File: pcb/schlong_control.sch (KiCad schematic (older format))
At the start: 38 parts, among them P1 Power Connector (120V AC), P2 Input, P3 Output, U1 74HC595, U2 MOC3063M, U3 MOC3063M, U4 MOC3063M, U5 MOC3063M, U6 MOC3063M, U7 LM7805

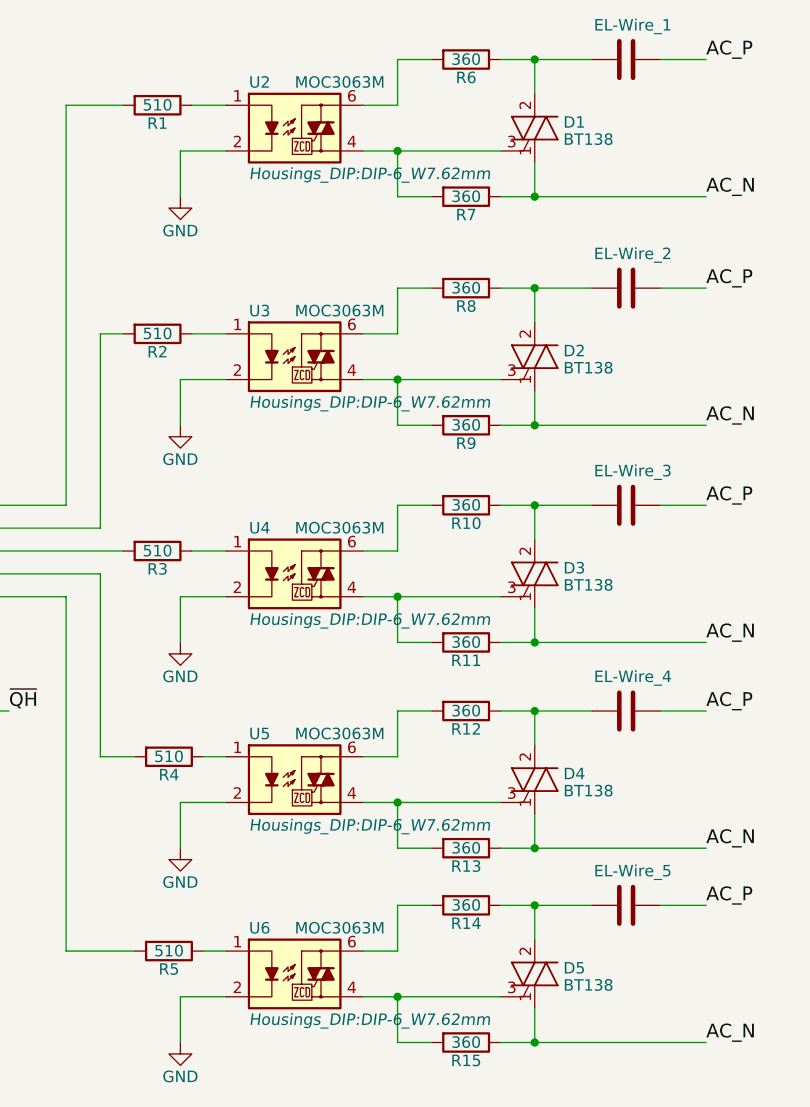
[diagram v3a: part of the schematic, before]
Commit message: shinkify pcb even more + little fixes
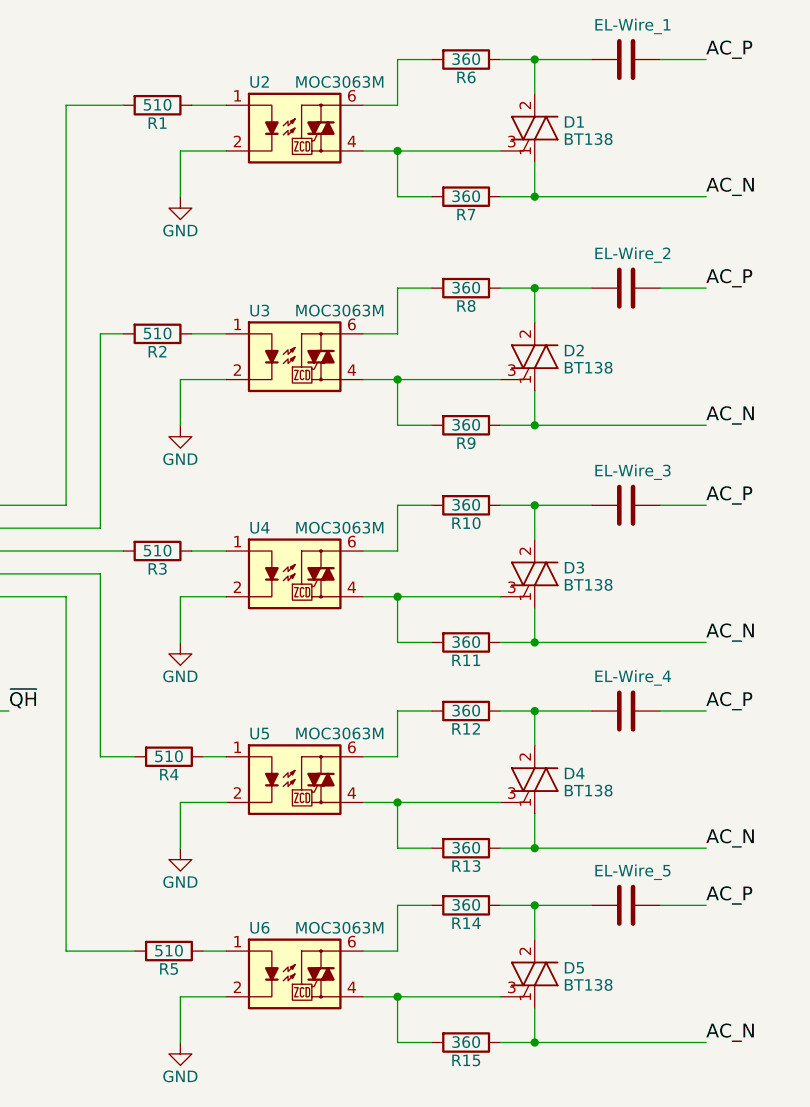
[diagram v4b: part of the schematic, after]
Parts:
- EL-Wire_1, EL-Wire_2, EL-Wire_3, EL-Wire_4, EL-Wire_5: footprint Connectors_Terminal_Blocks:TerminalBlock_Pheonix_MKDS1.5-2pol -> Connectors:PINHEAD1-2
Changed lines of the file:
@@
 EESchema Schematic File Version 2
-LIBS:schlong_control-rescue
 LIBS:power
 LIBS:device
@@
 LIBS:contrib
 LIBS:valves
+LIBS:bt138
+LIBS:7805_(enumerated_pins)
 LIBS:schlong_control-cache
 EELAYER 25 0
@@
 Sheet 1 1
 Title "Schlong Module Circuit"
-Date "2017-09-01"
-Rev "4"
+Date "2017-09-02"
+Rev "5"
 Comp "coon@c-base.org"
 Comment1 ""
@@
 F 0 "EL-Wire_1" V 6950 750 50  0000 L CNN
 F 1 "C" V 6850 800 50  0001 L CNN
-F 2 "Connectors_Terminal_Blocks:TerminalBlock_Pheonix_MKDS1.5-2pol" H 6838 800 50  0001 C CNN
+F 2 "Connectors:PINHEAD1-2" H 6838 800 50  0001 C CNN
 F 3 "" H 6800 950 50  0000 C CNN
 	1    6800 950
@@
 F 0 "EL-Wire_2" V 6950 1750 50  0000 L CNN
 F 1 "C" V 6850 1800 50  0001 L CNN
-F 2 "Connectors_Terminal_Blocks:TerminalBlock_Pheonix_MKDS1.5-2pol" H 6838 1800 50  0001 C CNN
+F 2 "Connectors:PINHEAD1-2" H 6838 1800 50  0001 C CNN
 F 3 "" H 6800 1950 50  0000 C CNN
 	1    6800 1950
@@
 F 0 "EL-Wire_3" V 6950 2700 50  0000 L CNN
 F 1 "C" V 6850 2750 50  0001 L CNN
-F 2 "Connectors_Terminal_Blocks:TerminalBlock_Pheonix_MKDS1.5-2pol" H 6838 2750 50  0001 C CNN
+F 2 "Connectors:PINHEAD1-2" H 6838 2750 50  0001 C CNN
 F 3 "" H 6800 2900 50  0000 C CNN
 	1    6800 2900
@@
 F 0 "EL-Wire_4" V 6950 3600 50  0000 L CNN
 F 1 "C" V 6850 3650 50  0001 L CNN
-F 2 "Connectors_Terminal_Blocks:TerminalBlock_Pheonix_MKDS1.5-2pol" H 6838 3650 50  0001 C CNN
+F 2 "Connectors:PINHEAD1-2" H 6838 3650 50  0001 C CNN
 F 3 "" H 6800 3800 50  0000 C CNN
 	1    6800 3800
@@
 F 0 "EL-Wire_5" V 6950 4450 50  0000 L CNN
 F 1 "C" V 6850 4500 50  0001 L CNN
-F 2 "Connectors_Terminal_Blocks:TerminalBlock_Pheonix_MKDS1.5-2pol" H 6838 4500 50  0001 C CNN
+F 2 "Connectors:PINHEAD1-2" H 6838 4500 50  0001 C CNN
 F 3 "" H 6800 4650 50  0000 C CNN
 	1    6800 4650
@@
 F 0 "U2" H 5150 1450 50  0000 L CNN
 F 1 "MOC3063M" H 5350 1450 50  0000 L CNN
-F 2 "Housings_DIP:DIP-6_W7.62mm" H 5150 1050 50  0000 L CIN
+F 2 "Housings_DIP:DIP-6_W7.62mm" H 5150 1050 50  0001 L CIN
 F 3 "" H 5340 1250 50  0000 L CNN
 	1    5350 1250
@@
 F 0 "U3" H 5150 2450 50  0000 L CNN
 F 1 "MOC3063M" H 5350 2450 50  0000 L CNN
-F 2 "Housings_DIP:DIP-6_W7.62mm" H 5150 2050 50  0000 L CIN
+F 2 "Housings_DIP:DIP-6_W7.62mm" H 5150 2050 50  0001 L CIN
 F 3 "" H 5340 2250 50  0000 L CNN
 	1    5350 2250
@@
 F 0 "U4" H 5150 3400 50  0000 L CNN
 F 1 "MOC3063M" H 5350 3400 50  0000 L CNN
-F 2 "Housings_DIP:DIP-6_W7.62mm" H 5150 3000 50  0000 L CIN
+F 2 "Housings_DIP:DIP-6_W7.62mm" H 5150 3000 50  0001 L CIN
 F 3 "" H 5340 3200 50  0000 L CNN
 	1    5350 3200
@@
 F 0 "U5" H 5150 4300 50  0000 L CNN
 F 1 "MOC3063M" H 5350 4300 50  0000 L CNN
-F 2 "Housings_DIP:DIP-6_W7.62mm" H 5150 3900 50  0000 L CIN
+F 2 "Housings_DIP:DIP-6_W7.62mm" H 5150 3900 50  0001 L CIN
 F 3 "" H 5340 4100 50  0000 L CNN
 	1    5350 4100
@@
 F 0 "U6" H 5150 5150 50  0000 L CNN
 F 1 "MOC3063M" H 5350 5150 50  0000 L CNN
-F 2 "Housings_DIP:DIP-6_W7.62mm" H 5150 4750 50  0000 L CIN
+F 2 "Housings_DIP:DIP-6_W7.62mm" H 5150 4750 50  0001 L CIN
 F 3 "" H 5340 4950 50  0000 L CNN
 	1    5350 4950

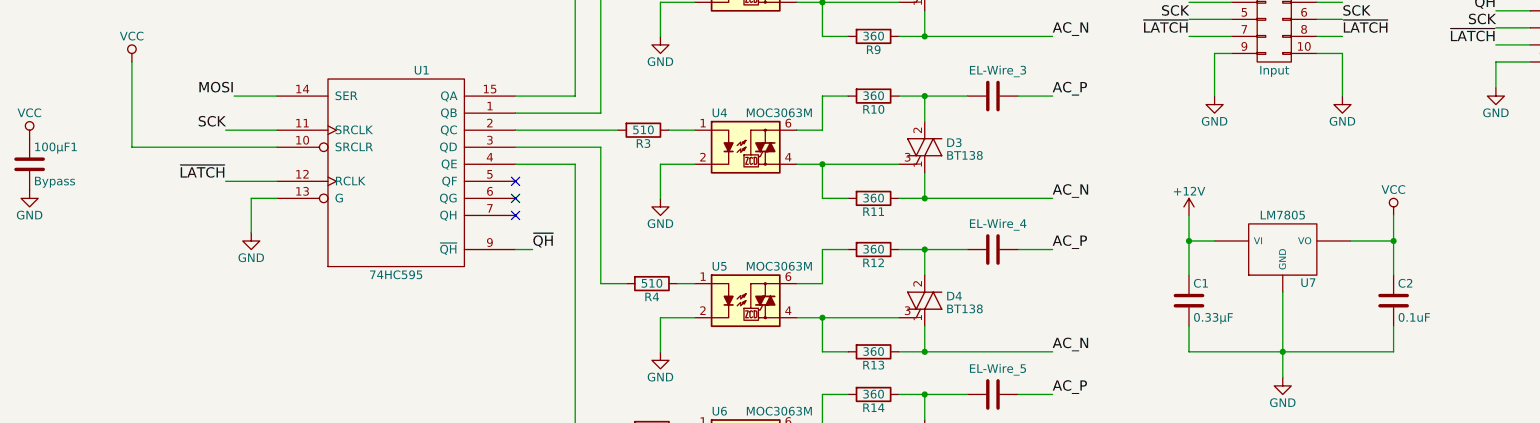
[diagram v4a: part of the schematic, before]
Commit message: redo routing (seperate logic voltage from AC voltage)
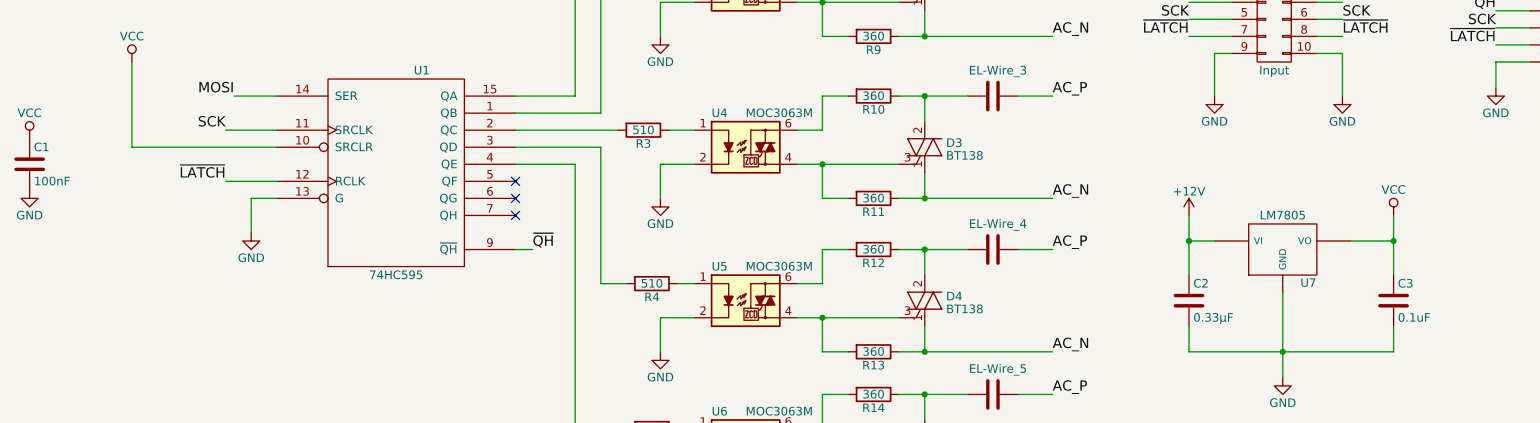
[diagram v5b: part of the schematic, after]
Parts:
- C1: renamed from 100µF1; value Bypass -> 100nF; footprint Capacitors_THT:C_Disc_D3.0mm_W1.6mm_P2.50mm -> Capacitors_ThroughHole:C_Disc_D3.0mm_W1.6mm_P2.50mm
- C2: renamed from C1; footprint Capacitors_THT:CP_Radial_D4.0mm_P1.50mm -> Capacitors_ThroughHole:CP_Radial_D4.0mm_P1.50mm
- C3: renamed from C2; footprint Capacitors_THT:CP_Radial_D4.0mm_P1.50mm -> Capacitors_ThroughHole:CP_Radial_D4.0mm_P1.50mm
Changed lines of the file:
@@
 AC_P
 $Comp
-L GND #PWR01
+L GND #PWR5
 U 1 1 58A93B28
 P 4850 1550
-F 0 "#PWR01" H 4850 1300 50  0001 C CNN
+F 0 "#PWR5" H 4850 1300 50  0001 C CNN
 F 1 "GND" H 4850 1400 50  0000 C CNN
 F 2 "" H 4850 1550 50  0000 C CNN
@@
 AC_P
 $Comp
-L GND #PWR02
+L GND #PWR6
 U 1 1 58A941CA
 P 4850 2550
-F 0 "#PWR02" H 4850 2300 50  0001 C CNN
+F 0 "#PWR6" H 4850 2300 50  0001 C CNN
 F 1 "GND" H 4850 2400 50  0000 C CNN
 F 2 "" H 4850 2550 50  0000 C CNN
@@
 AC_P
 $Comp
-L GND #PWR03
+L GND #PWR7
 U 1 1 58A94296
 P 4850 3500
-F 0 "#PWR03" H 4850 3250 50  0001 C CNN
+F 0 "#PWR7" H 4850 3250 50  0001 C CNN
 F 1 "GND" H 4850 3350 50  0000 C CNN
 F 2 "" H 4850 3500 50  0000 C CNN
@@
 AC_P
 $Comp
-L GND #PWR04
+L GND #PWR8
 U 1 1 58A94373
 P 4850 4400
-F 0 "#PWR04" H 4850 4150 50  0001 C CNN
+F 0 "#PWR8" H 4850 4150 50  0001 C CNN
 F 1 "GND" H 4850 4250 50  0000 C CNN
 F 2 "" H 4850 4400 50  0000 C CNN
@@
 AC_P
 $Comp
-L GND #PWR05
+L GND #PWR9
 U 1 1 58A94836
 P 4850 5250
-F 0 "#PWR05" H 4850 5000 50  0001 C CNN
+F 0 "#PWR9" H 4850 5000 50  0001 C CNN
 F 1 "GND" H 4850 5100 50  0000 C CNN
 F 2 "" H 4850 5250 50  0000 C CNN
@@
 NoConn ~ 4000 3600
 $Comp
-L VCC #PWR06
+L VCC #PWR3
 U 1 1 58A979A6
 P 1750 2700
-F 0 "#PWR06" H 1750 2550 50  0001 C CNN
+F 0 "#PWR3" H 1750 2550 50  0001 C CNN
 F 1 "VCC" H 1750 2850 50  0000 C CNN
 F 2 "" H 1750 2700 50  0000 C CNN
@@
 $EndComp
 $Comp
-L GND #PWR07
+L GND #PWR4
 U 1 1 58A98202
 P 2450 3700
-F 0 "#PWR07" H 2450 3450 50  0001 C CNN
+F 0 "#PWR4" H 2450 3450 50  0001 C CNN
 F 1 "GND" H 2450 3550 50  0000 C CNN
 F 2 "" H 2450 3700 50  0000 C CNN
@@
 $EndComp
 $Comp
-L PWR_FLAG #FLG08
+L PWR_FLAG #FLG2
 U 1 1 58A91E89
 P 10550 1300
-F 0 "#FLG08" H 10550 1395 50  0001 C CNN
+F 0 "#FLG2" H 10550 1395 50  0001 C CNN
 F 1 "PWR_FLAG" H 10550 1480 50  0000 C CNN
 F 2 "" H 10550 1300 50  0000 C CNN
@@
 $EndComp
 $Comp
-L GND #PWR09
+L GND #PWR20
 U 1 1 58A9369D
 P 10550 1450
-F 0 "#PWR09" H 10550 1200 50  0001 C CNN
+F 0 "#PWR20" H 10550 1200 50  0001 C CNN
 F 1 "GND" H 10550 1300 50  0000 C CNN
 F 2 "" H 10550 1450 50  0000 C CNN
@@
 $EndComp
 $Comp
-L GND #PWR010
+L GND #PWR12
 U 1 1 58C9F740
 P 8100 2900
-F 0 "#PWR010" H 8100 2650 50  0001 C CNN
+F 0 "#PWR12" H 8100 2650 50  0001 C CNN
 F 1 "GND" H 8100 2750 50  0000 C CNN
 F 2 "" H 8100 2900 50  0000 C CNN
@@
 ~LATCH
 $Comp
-L +12V #PWR011
+L +12V #PWR18
 U 1 1 58CA41A9
 P 9750 2200
-F 0 "#PWR011" H 9750 2050 50  0001 C CNN
+F 0 "#PWR18" H 9750 2050 50  0001 C CNN
 F 1 "+12V" H 9750 2340 50  0000 C CNN
 F 2 "" H 9750 2200 50  0000 C CNN
@@
 ~LATCH
 $Comp
-L GND #PWR012
+L GND #PWR19
 U 1 1 58CA466D
 P 9750 2850
-F 0 "#PWR012" H 9750 2600 50  0001 C CNN
+F 0 "#PWR19" H 9750 2600 50  0001 C CNN
 F 1 "GND" H 9750 2700 50  0000 C CNN
 F 2 "" H 9750 2850 50  0000 C CNN
@@
 Wire Wire Line
 	6950 1950 7150 1950
-Wire Wire Line
-	5800 3100 5650 3100
-Wire Wire Line
-	5650 3300 6250 3300
 Connection ~ 6400 2900
 Wire Wire Line
 	6400 3050 6400 2900
 Wire Wire Line
-	5800 3100 5800 2900
-Wire Wire Line
-	5800 2900 5950 2900
-Wire Wire Line
 	6400 3350 6400 3500
-Wire Wire Line
-	5050 3300 4850 3300
 Wire Wire Line
 	6250 2900 6650 2900
@@
 	4900 2150 5050 2150
 Wire Wire Line
-	4900 3100 5050 3100
-Wire Wire Line
 	4000 3100 4600 3100
 Wire Wire Line
@@
 	5800 4400 5950 4400
 Connection ~ 5800 4200
-Wire Wire Line
-	5800 3300 5800 3500
-Wire Wire Line
-	5800 3500 5950 3500
-Connection ~ 5800 3300
 Wire Wire Line
 	5800 2350 5800 2550
@@
 	9750 2700 9750 2850
 $Comp
-L +12V #PWR013
+L +12V #PWR14
 U 1 1 58CA520E
 P 8800 2100
-F 0 "#PWR013" H 8800 1950 50  0001 C CNN
+F 0 "#PWR14" H 8800 1950 50  0001 C CNN
 F 1 "+12V" H 8800 2240 50  0000 C CNN
 F 2 "" H 8800 2100 50  0000 C CNN
@@
 	8800 2250 8800 2100
 $Comp
-L +12V #PWR014
+L +12V #PWR11
 U 1 1 58C9DC98
 P 8100 2100
-F 0 "#PWR014" H 8100 1950 50  0001 C CNN
+F 0 "#PWR11" H 8100 1950 50  0001 C CNN
 F 1 "+12V" H 8100 2240 50  0000 C CNN
 F 2 "" H 8100 2100 50  0000 C CNN
@@
 ~LATCH
 $Comp
-L GND #PWR015
+L GND #PWR15
 U 1 1 58CA601F
 P 8850 2900
-F 0 "#PWR015" H 8850 2650 50  0001 C CNN
+F 0 "#PWR15" H 8850 2650 50  0001 C CNN
 F 1 "GND" H 8850 2750 50  0000 C CNN
 F 2 "" H 8850 2900 50  0000 C CNN
@@
 	8700 2350 8850 2350
 $Comp
-L +12V #PWR016
+L +12V #PWR21
 U 1 1 58CA7930
 P 10700 2200
-F 0 "#PWR016" H 10700 2050 50  0001 C CNN
+F 0 "#PWR21" H 10700 2050 50  0001 C CNN
 F 1 "+12V" H 10700 2340 50  0000 C CNN
 F 2 "" H 10700 2200 50  0000 C CNN
@@
 	10700 2200 10700 2300
 $Comp
-L GND #PWR017
+L GND #PWR22
 U 1 1 58CA7CF1
 P 10700 2850
-F 0 "#PWR017" H 10700 2600 50  0001 C CNN
+F 0 "#PWR22" H 10700 2600 50  0001 C CNN
 F 1 "GND" H 10700 2700 50  0000 C CNN
 F 2 "" H 10700 2850 50  0000 C CNN
@@
 	9750 2400 9950 2400
 $Comp
-L +12V #PWR018
+L +12V #PWR16
 U 1 1 58CAB532
 P 9000 1250
-F 0 "#PWR018" H 9000 1100 50  0001 C CNN
+F 0 "#PWR16" H 9000 1100 50  0001 C CNN
 F 1 "+12V" H 9000 1390 50  0000 C CNN
 F 2 "" H 9000 1250 50  0000 C CNN
@@
 $EndComp
 $Comp
-L PWR_FLAG #FLG019
+L PWR_FLAG #FLG1
 U 1 1 58CAB634
 P 9350 1300
-F 0 "#FLG019" H 9350 1395 50  0001 C CNN
+F 0 "#FLG1" H 9350 1395 50  0001 C CNN
 F 1 "PWR_FLAG" H 9350 1480 50  0000 C CNN
 F 2 "" H 9350 1300 50  0000 C CNN
@@
 	9350 1400 9350 1300
 $Comp
-L +12V #PWR020
+L +12V #PWR10
 U 1 1 58CAEF1E
 P 7950 3600
-F 0 "#PWR020" H 7950 3450 50  0001 C CNN
+F 0 "#PWR10" H 7950 3450 50  0001 C CNN
 F 1 "+12V" H 7950 3740 50  0000 C CNN
 F 2 "" H 7950 3600 50  0000 C CNN
@@
 	7950 3750 8100 3750
 $Comp
-L GND #PWR021
+L GND #PWR13
 U 1 1 58CAF198
 P 8500 4550
-F 0 "#PWR021" H 8500 4300 50  0001 C CNN
+F 0 "#PWR13" H 8500 4300 50  0001 C CNN
 F 1 "GND" H 8500 4400 50  0000 C CNN
 F 2 "" H 8500 4550 50  0000 C CNN
@@
 	8500 4050 8500 4550
 $Comp
-L VCC #PWR022
+L VCC #PWR17
 U 1 1 58CAF4F3
 P 9150 3600
-F 0 "#PWR022" H 9150 3450 50  0001 C CNN
+F 0 "#PWR17" H 9150 3450 50  0001 C CNN
 F 1 "VCC" H 9150 3750 50  0000 C CNN
 F 2 "" H 9150 3600 50  0000 C CNN
@@
 	8900 3750 9150 3750
 $Comp
-L C C1
+L C C2
 U 1 1 58CB259E
 P 7950 4100
-F 0 "C1" H 7975 4200 50  0000 L CNN
+F 0 "C2" H 7975 4200 50  0000 L CNN
 F 1 "0.33µF" H 7975 4000 50  0000 L CNN
-F 2 "Capacitors_THT:CP_Radial_D4.0mm_P1.50mm" H 7988 3950 50  0001 C CNN
+F 2 "Capacitors_ThroughHole:CP_Radial_D4.0mm_P1.50mm" H 7988 3950 50  0001 C CNN
 F 3 "" H 7950 4100 50  0000 C CNN
 	1    7950 4100
@@
 $EndComp
 $Comp
-L C 100µF1
+L C C1
 U 1 1 58CEB671
 P 1150 3300
-F 0 "100µF1" H 1175 3400 50  0000 L CNN
-F 1 "Bypass" H 1175 3200 50  0000 L CNN
-F 2 "Capacitors_THT:C_Disc_D3.0mm_W1.6mm_P2.50mm" H 1188 3150 50  0001 C CNN
+F 0 "C1" H 1175 3400 50  0000 L CNN
+F 1 "100nF" H 1175 3200 50  0000 L CNN
+F 2 "Capacitors_ThroughHole:C_Disc_D3.0mm_W1.6mm_P2.50mm" H 1188 3150 50  0001 C CNN
 F 3 "" H 1150 3300 50  0000 C CNN
 	1    1150 3300
@@
 $EndComp
 $Comp
-L VCC #PWR023
+L VCC #PWR1
 U 1 1 58CEBA80
 P 1150 3150
-F 0 "#PWR023" H 1150 3000 50  0001 C CNN
+F 0 "#PWR1" H 1150 3000 50  0001 C CNN
 F 1 "VCC" H 1150 3300 50  0000 C CNN
 F 2 "" H 1150 3150 50  0000 C CNN
@@
 $EndComp
 $Comp
-L GND #PWR024
+L GND #PWR2
 U 1 1 58CEBADE
 P 1150 3450
-F 0 "#PWR024" H 1150 3200 50  0001 C CNN
+F 0 "#PWR2" H 1150 3200 50  0001 C CNN
 F 1 "GND" H 1150 3300 50  0000 C CNN
 F 2 "" H 1150 3450 50  0000 C CNN
@@
 $EndComp
 $Comp
-L C C2
+L C C3
 U 1 1 59A9C281
 P 9150 4100
-F 0 "C2" H 9175 4200 50  0000 L CNN
+F 0 "C3" H 9175 4200 50  0000 L CNN
 F 1 "0.1uF" H 9175 4000 50  0000 L CNN
-F 2 "Capacitors_THT:CP_Radial_D4.0mm_P1.50mm" H 9188 3950 50  0001 C CNN
+F 2 "Capacitors_ThroughHole:CP_Radial_D4.0mm_P1.50mm" H 9188 3950 50  0001 C CNN
 F 3 "" H 9150 4100 50  0001 C CNN
 	1    9150 4100
@@
 Wire Wire Line
 	9150 4400 9150 4250
+Wire Wire Line
+	4900 3100 5050 3100
+Wire Wire Line
+	4850 3300 5050 3300
+Wire Wire Line
+	5650 3100 5800 3100
+Wire Wire Line
+	5800 3100 5800 2900
+Wire Wire Line
+	5800 2900 5950 2900
+Wire Wire Line
+	5650 3300 6250 3300
+Wire Wire Line
+	5950 3500 5800 3500
+Wire Wire Line
+	5800 3500 5800 3300
+Connection ~ 5800 3300
 $EndSCHEMATC

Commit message: rework design
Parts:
- added P1: Power Input (120V AC), TerminalBlocks_Phoenix:TerminalBlock_Phoenix_MKDS1.5-2pol, symbol CONN_01X02
- added R1, R2, R3: 4k7, Resistors_THT:R_Axial_DIN0207_L6.3mm_D2.5mm_P7.62mm_Horizontal, symbol R
- P2: renamed from P1; value Power Connector (120V AC) -> Power Thru (120V AC); footprint Connectors_Terminal_Blocks:TerminalBlock_Pheonix_MKDS1.5-2pol -> TerminalBlocks_Phoenix:TerminalBlock_Phoenix_MKDS1.5-2pol
- P3: renamed from P2; footprint Connectors:IDC_Header_Straight_10pins -> idc:IDC_Header_Straight_2x05_Pitch2.54mm
- P4: renamed from P3; footprint Connectors:IDC_Header_Straight_10pins -> idc:IDC_Header_Straight_2x05_Pitch2.54mm
- renumbered R7 to R10, R8 to R11, R9 to R12, R10 to R13, R11 to R14, R12 to R15, R13 to R16, R14 to R17, R15 to R18, R1 to R4, R2 to R5, R3 to R6, R4 to R7, R5 to R8, R6 to R9
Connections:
- net AC_N: now also P1.2 (P2)
- net AC_P: now also P1.1 (P1)
- net GND: now also R1.2, R2.2, R3.2
- net MOSI: now also R3.1
- net SCK: now also R1.1
- net ~LATCH: now also R2.1
